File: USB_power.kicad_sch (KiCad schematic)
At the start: 24 parts, among them J4 TYPE-C-31-M12_13, J5 JST-4-pin, Q1 Q_NMOS, U3 TPD4E05U06DQAR, U4 BQ24074RGTR

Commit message: Power supply and PCB stuff
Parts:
- removed TH1: 10k, keyboard:R_0402_1005Metric, symbol keyboard:Thermistor_NTC
- added R20: R_US, keyboard:R_0402_1005Metric, symbol keyboard:R_US
- R12: value 8k2 -> VAL
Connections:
- net GND: now also R20.2
- net at U4.1 (TS): now also R20.1
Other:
- note added: "Make it DNP to set default Termination current of 10% charge current"
- note added: "TS pin is for batt pack thermistor. Connect to GND through 10k res if a thermistor is not used. Rilim (R11) sets Input current limit. 1.1k - 8k Ohms Iinmax = Kilim/Rilim (Kilim: 1500-1720, 1610typ) TMR pin left unconnected to set default timings for pre-charge and fast charge timings. Riset (R12) sets charge current limit. 590 - 8.9k Ohms Ichg = Kiset/Riset (Kiset: 797-975, 890typ)"
- note added: "There are 3 charger IC which are functionally compatibility. BQ24073, BQ24074, BQ24075. Any one of them can be used. They are all pin to pin compatible and the design is done in such a way that you can swap out one for another on same PCB and have same functionality."
- note removed: "Make it DNP to set default Termination current"
- note removed: "Rilim (R4) = 1.2k sets Input current limit to 1.3A. TMR pin left unconnected to set default timings for pre-charge and fast charge timings. Riset (R3) = 8.2k sets batt fast charge current limit to 100mA."
- note removed: "Theere are 3 charger IC which are functionally compatibility. BQ24073, BQ24074, BQ24075. Any one of thrm can be used. They are all pin to pin compatible and the design is done in such a way that you can swap out one for another on same PCB and have same functionality."
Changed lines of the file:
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@@
 		)
 	)
-	(text "Theere are 3 charger IC which are\nfunctionally compatibility.\nBQ24073, BQ24074, BQ24075.\nAny one of thrm can be used.\nThey are all pin to pin compatible \nand the design is done in such a way\nthat you can swap out one for another \non same PCB and have same functionality."
+	(text "There are 3 charger IC which are\nfunctionally compatibility.\nBQ24073, BQ24074, BQ24075.\nAny one of them can be used.\nThey are all pin to pin compatible \nand the design is done in such a way\nthat you can swap out one for another \non same PCB and have same functionality."
 		(exclude_from_sim no)
-		(at 113.03 103.632 0)
+		(at 113.792 102.362 0)
 		(effects
 			(font
@@
 		)
 	)
-	(text "Rilim (R4) = 1.2k sets \nInput current \nlimit to 1.3A.\n\nTMR pin left unconnected \nto set default timings \nfor pre-charge and fast charge\ntimings.\n\nRiset (R3) = 8.2k sets \nbatt fast charge \ncurrent limit to 100mA."
+	(text "TS pin is for batt pack thermistor.\nConnect to GND through 10k res if\na thermistor is not used.\n\nRilim (R11) sets Input\ncurrent limit. 1.1k - 8k Ohms\nIinmax = Kilim/Rilim\n(Kilim: 1500-1720, 1610typ)\n\nTMR pin left unconnected \nto set default timings \nfor pre-charge and fast charge\ntimings.\n\nRiset (R12) sets charge\ncurrent limit. 590 - 8.9k Ohms\nIchg = Kiset/Riset (Kiset: 797-975, 890typ)"
 		(exclude_from_sim no)
-		(at 51.054 150.622 0)
+		(at 49.784 148.59 0)
 		(effects
 			(font
@@
 		)
 	)
-	(text "Make it DNP to set default Termination current"
+	(text "Make it DNP to set default Termination current\nof 10% charge current"
 		(exclude_from_sim no)
 		(at 168.148 152.654 0)
@@
 	)
 	(symbol
-		(lib_id "keyboard:Thermistor_NTC")
-		(at 105.41 119.38 270)
-		(unit 1)
-		(exclude_from_sim no)
-		(in_bom yes)
-		(on_board yes)
-		(dnp no)
-		(property "Reference" "TH1"
-			(at 109.22 115.57 90)
-			(effects
-				(font
-					(size 1.27 1.27)
-				)
-			)
-		)
-		(property "Value" "10k"
-			(at 102.87 115.57 90)
-			(effects
-				(font
-					(size 1.27 1.27)
-				)
-			)
-		)
-		(property "Footprint" "keyboard:R_0402_1005Metric"
-			(at 106.68 119.38 0)
-			(effects
-				(font
-					(size 1.27 1.27)
-				)
-				(hide yes)
-			)
-		)
-		(property "Datasheet" "https://datasheet.lcsc.com/lcsc/2110081230_Sunlord-SDNT1005X103F3950FTF_C95939.pdf"
-			(at 106.68 119.38 0)
-			(effects
-				(font
-					(size 1.27 1.27)
-				)
-				(hide yes)
-			)
-		)
-		(property "Description" ""
-			(at 105.41 119.38 0)
-			(effects
-				(font
-					(size 1.27 1.27)
-				)
-				(hide yes)
-			)
-		)
-		(property "PN" "SDNT1005X103F3950FTF"
-			(at 105.41 119.38 0)
-			(effects
-				(font
-					(size 1.27 1.27)
-				)
-				(hide yes)
-			)
-		)
-		(property "LCSC Part Number" "C95939"
-			(at 105.41 119.38 0)
-			(effects
-				(font
-					(size 1.27 1.27)
-				)
-				(hide yes)
-			)
-		)
-		(property "LCSC link" "https://www.lcsc.com/product-detail/span-style-background-color-ff0-NTC-span-Thermistors_Sunlord-SDNT1005X103F3950FTF_C95939.html"
-			(at 105.41 119.38 0)
-			(effects
-				(font
-					(size 1.27 1.27)
-				)
-				(hide yes)
-			)
-		)
-		(pin "1"
-		)
-		(pin "2"
-		)
-		(instances
-			(project "Keyboard_60%"
-				(path "/ef112b03-6536-453f-8127-17d1495b48aa/01d5aa47-03a0-4747-998b-393b2b88e5ef"
-					(reference "TH1")
-					(unit 1)
-				)
-			)
-		)
-	)
-	(symbol
 		(lib_id "Unified-Daughterboard-rescue:TYPE-C-31-M12_13-acheronSymbols")
 		(at 49.53 53.34 0)
@@
 	)
 	(symbol
+		(lib_id "keyboard:R_US")
+		(at 105.41 119.38 0)
+		(unit 1)
+		(exclude_from_sim no)
+		(in_bom yes)
+		(on_board yes)
+		(dnp no)
+		(property "Reference" "R20"
+			(at 105.41 116.84 0)
+			(effects
+				(font
+					(size 1.27 1.27)
+				)
+			)
+		)
+		(property "Value" "R_US"
+			(at 105.41 121.92 0)
+			(effects
+				(font
+					(size 1.27 1.27)
+				)
+			)
+		)
+		(property "Footprint" "keyboard:R_0402_1005Metric"
+			(at 105.156 120.396 0)
+			(effects
+				(font
+					(size 1.27 1.27)
+				)
+				(hide yes)
+			)
+		)
+		(property "Datasheet" "https://datasheet.lcsc.com/lcsc/2304140030_YAGEO-RC0402FR-071K2L_C138040.pdf"
+			(at 105.41 119.38 90)
+			(effects
+				(font
+					(size 1.27 1.27)
+				)
+				(hide yes)
+			)
+		)
+		(property "Description" ""
+			(at 105.41 119.38 0)
+			(effects
+				(font
+					(size 1.27 1.27)
+				)
+				(hide yes)
+			)
+		)
+		(property "PN" "RC0402FR-071K2L"
+			(at 105.41 119.38 0)
+			(effects
+				(font
+					(size 1.27 1.27)
+				)
+				(hide yes)
+			)
+		)
+		(property "LCSC Part Number" "C138040"
+			(at 105.41 119.38 0)
+			(effects
+				(font
+					(size 1.27 1.27)
+				)
+				(hide yes)
+			)
+		)
+		(property "LCSC link" "https://www.lcsc.com/product-detail/Chip-Resistor-Surface-Mount_YAGEO-RC0402FR-071K2L_C138040.html"
+			(at 105.41 119.38 0)
+			(effects
+				(font
+					(size 1.27 1.27)
+				)
+				(hide yes)
+			)
+		)
+		(pin "1"
+		)
+		(pin "2"
+		)
+		(instances
+			(project "zmk-g915"
+				(path "/ef112b03-6536-453f-8127-17d1495b48aa/01d5aa47-03a0-4747-998b-393b2b88e5ef"
+					(reference "R20")
+					(unit 1)
+				)
+			)
+		)
+	)
+	(symbol
 		(lib_id "keyboard:JST-4-pin")
 		(at 135.89 59.69 0)
@@
 			)
 		)
-		(property "Value" "8k2"
+		(property "Value" "VAL"
 			(at 113.03 137.16 0)
 			(effects

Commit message: led matrix sheet
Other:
- company: HW-tinkerers -> (none)
- title: USB and Power Path  -> (none)
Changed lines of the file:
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@@
 	(generator_version "9.0")
 	(paper "A4")
-	(title_block
-		(title "USB and Power Path ")
-		(date "2024-02-17")
-		(rev "1.0")
-		(company "HW-tinkerers")
-	)
 	(text "Use accurate resistors (<1%)"
 		(exclude_from_sim no)

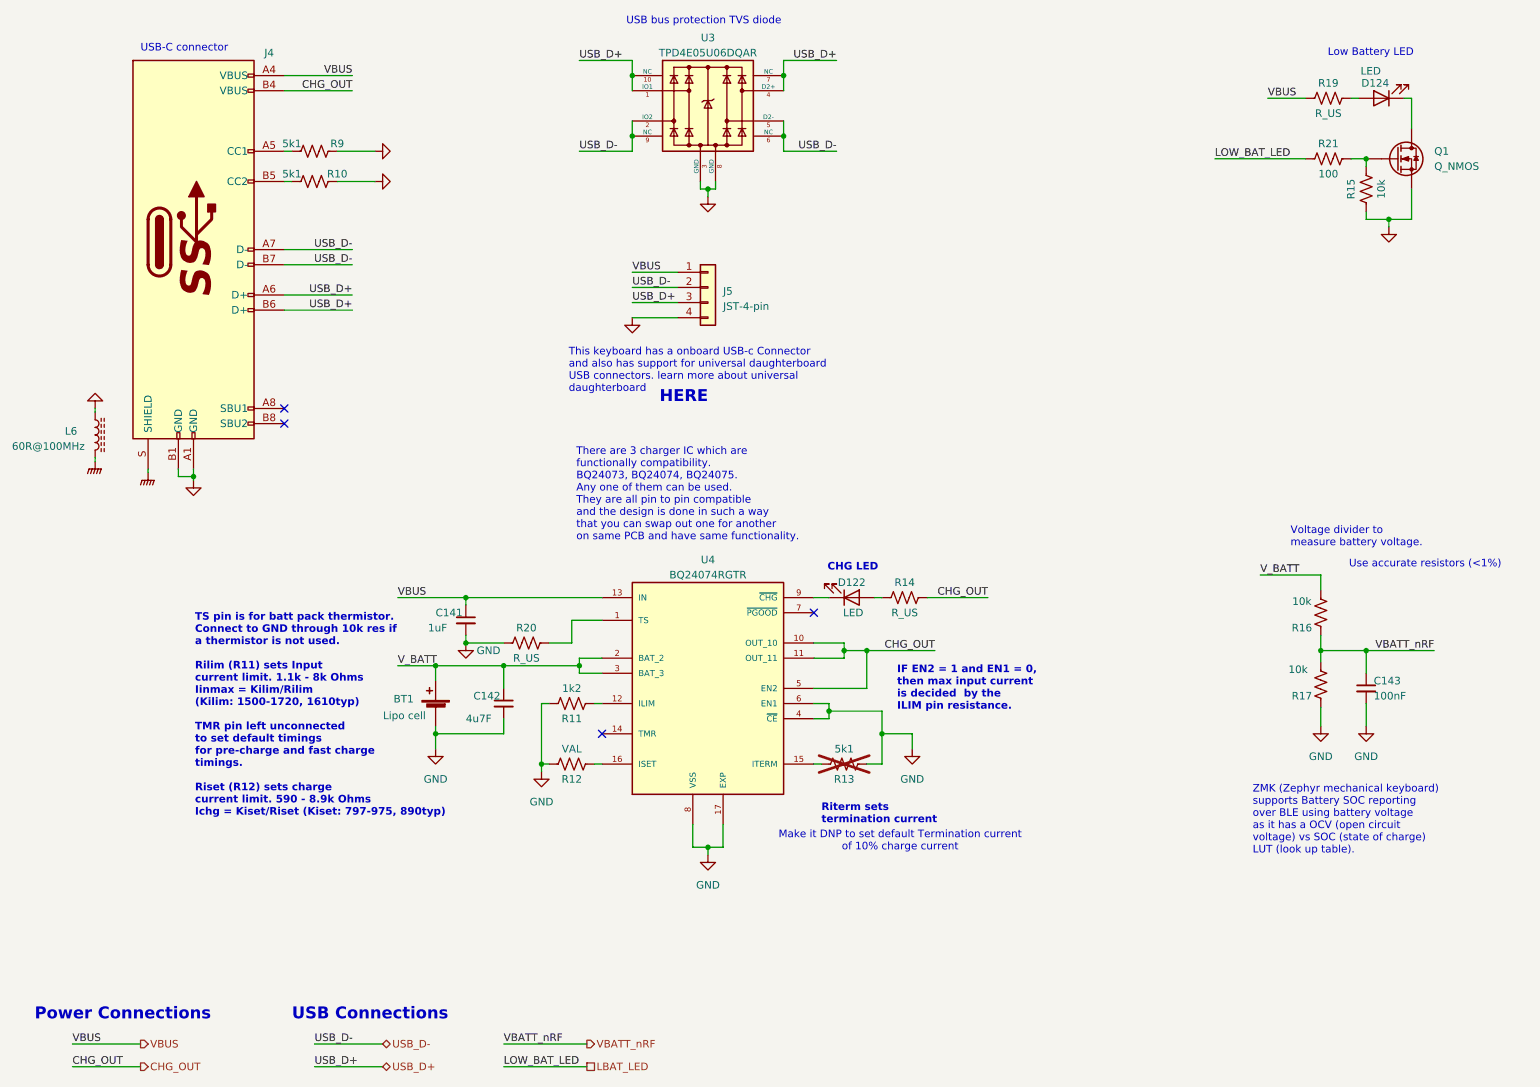
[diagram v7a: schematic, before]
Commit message: g915 and k618 pcb key and cutout placement
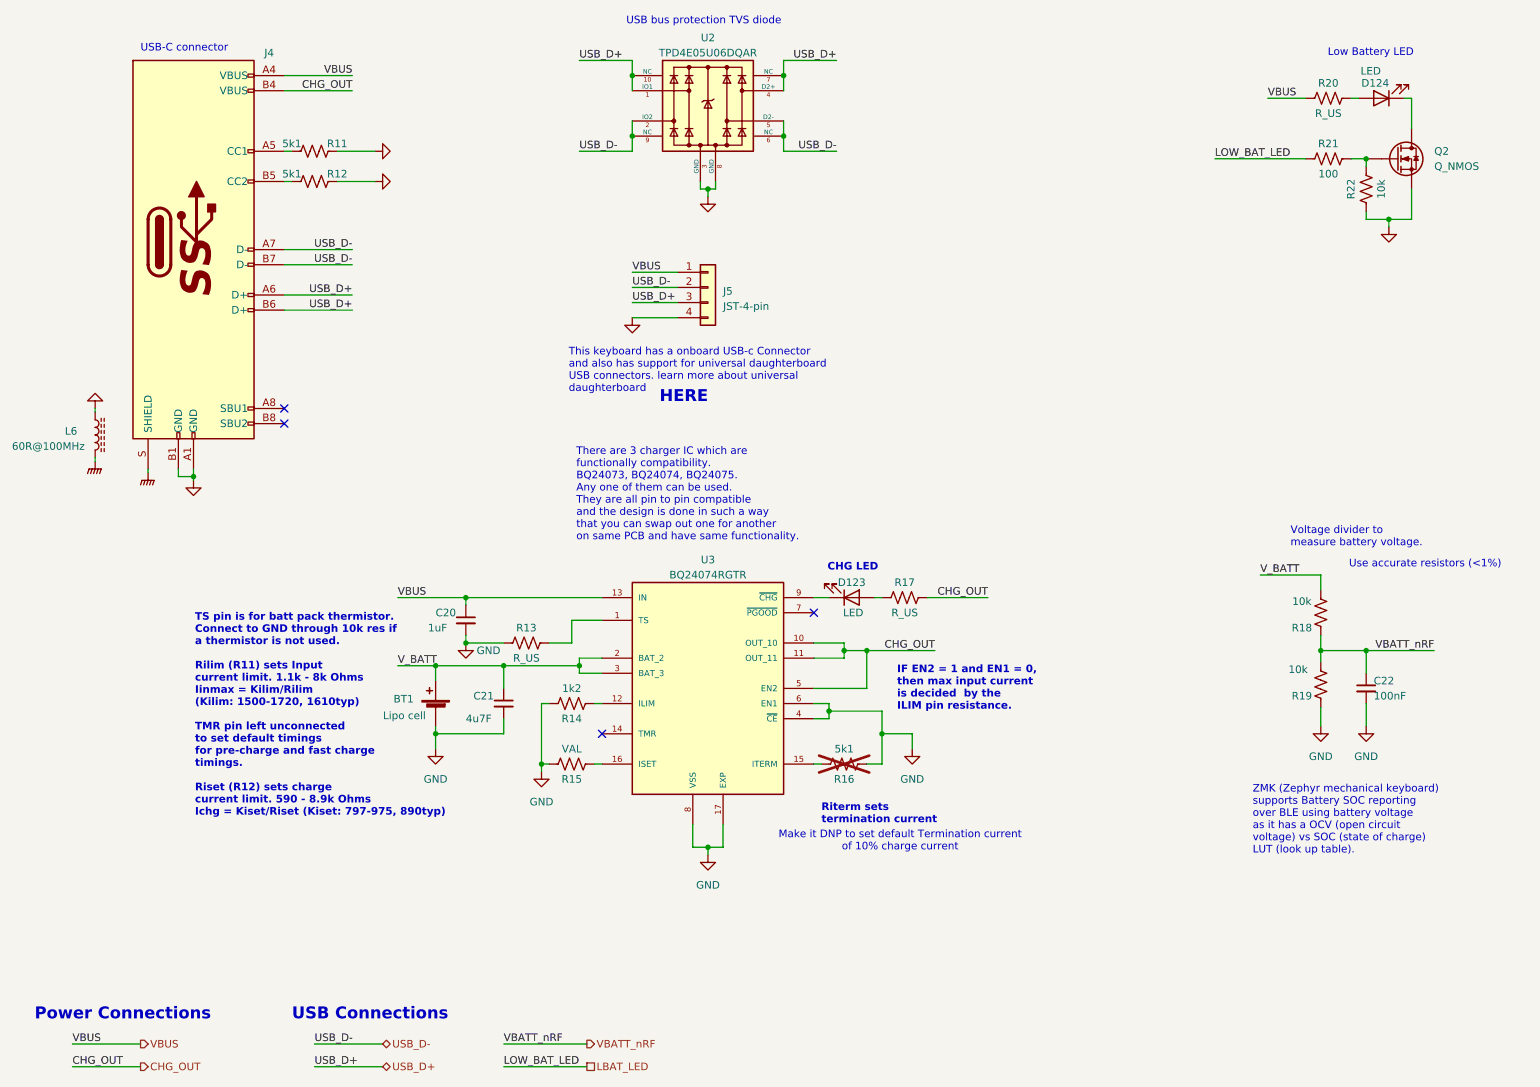
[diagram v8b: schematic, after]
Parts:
- renumbered C141 to C20, C142 to C21, C143 to C22, D122 to D123, Q1 to Q2, R9 to R11, R10 to R12, R20 to R13, R11 to R14, R12 to R15, R13 to R16, R14 to R17, R16 to R18, R17 to R19, R19 to R20, R15 to R22, U3 to U2, U4 to U3
